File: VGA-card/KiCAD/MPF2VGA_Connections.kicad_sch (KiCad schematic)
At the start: 7 parts, among them J1 AppleIIBus, J2 VGA, J3 VGA, SW1 SW_Push

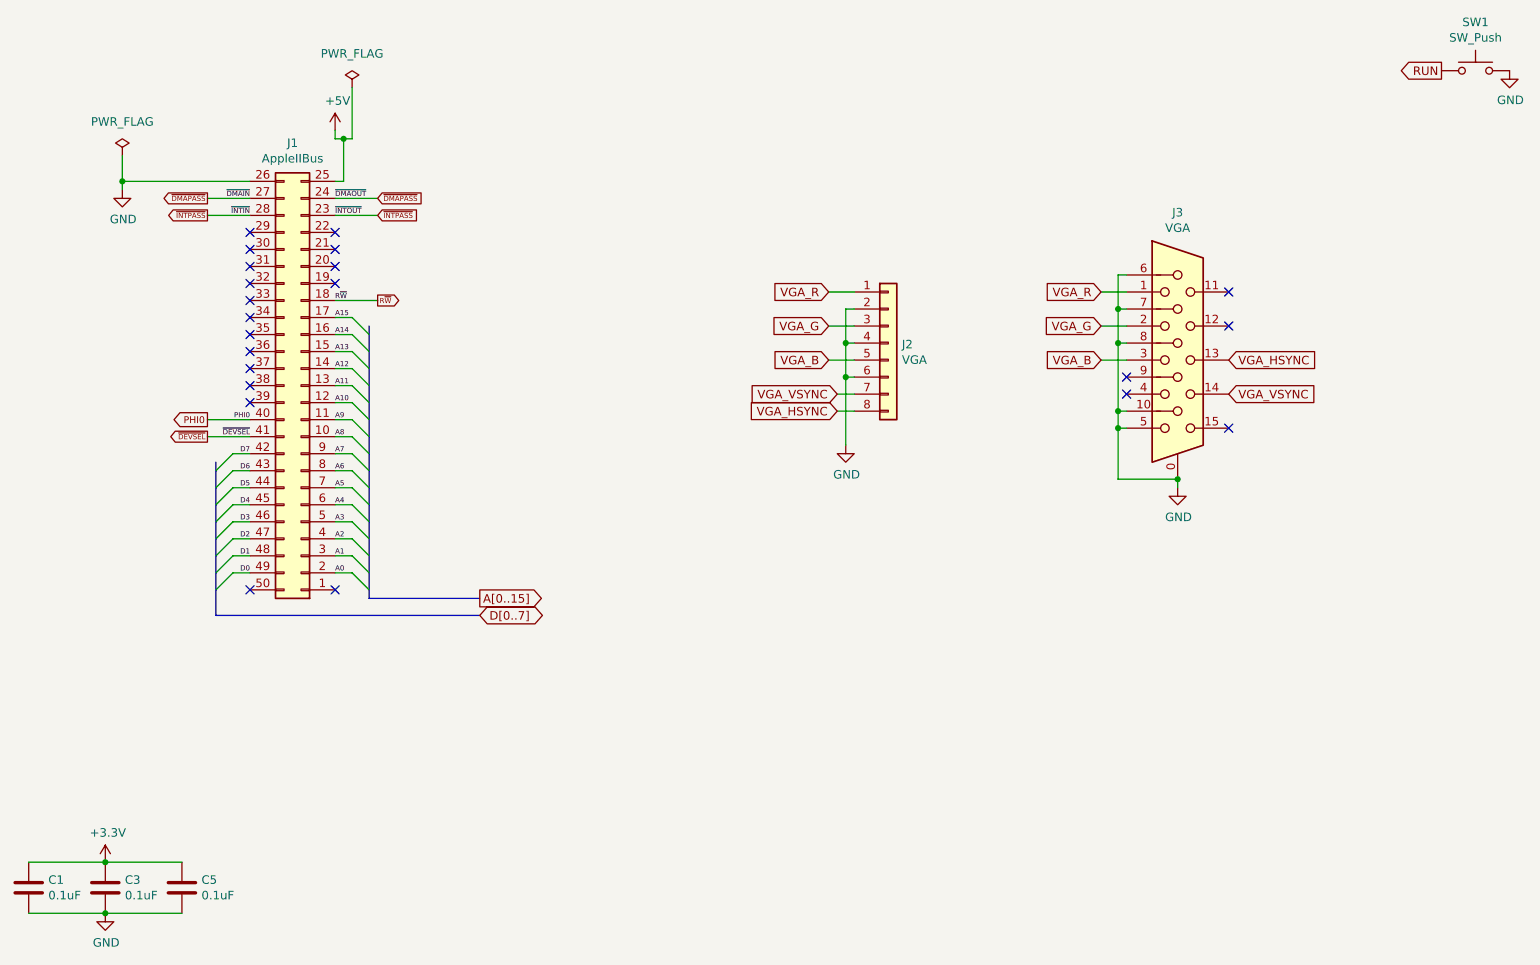
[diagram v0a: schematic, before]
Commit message: KiCAD connections sheet renamed
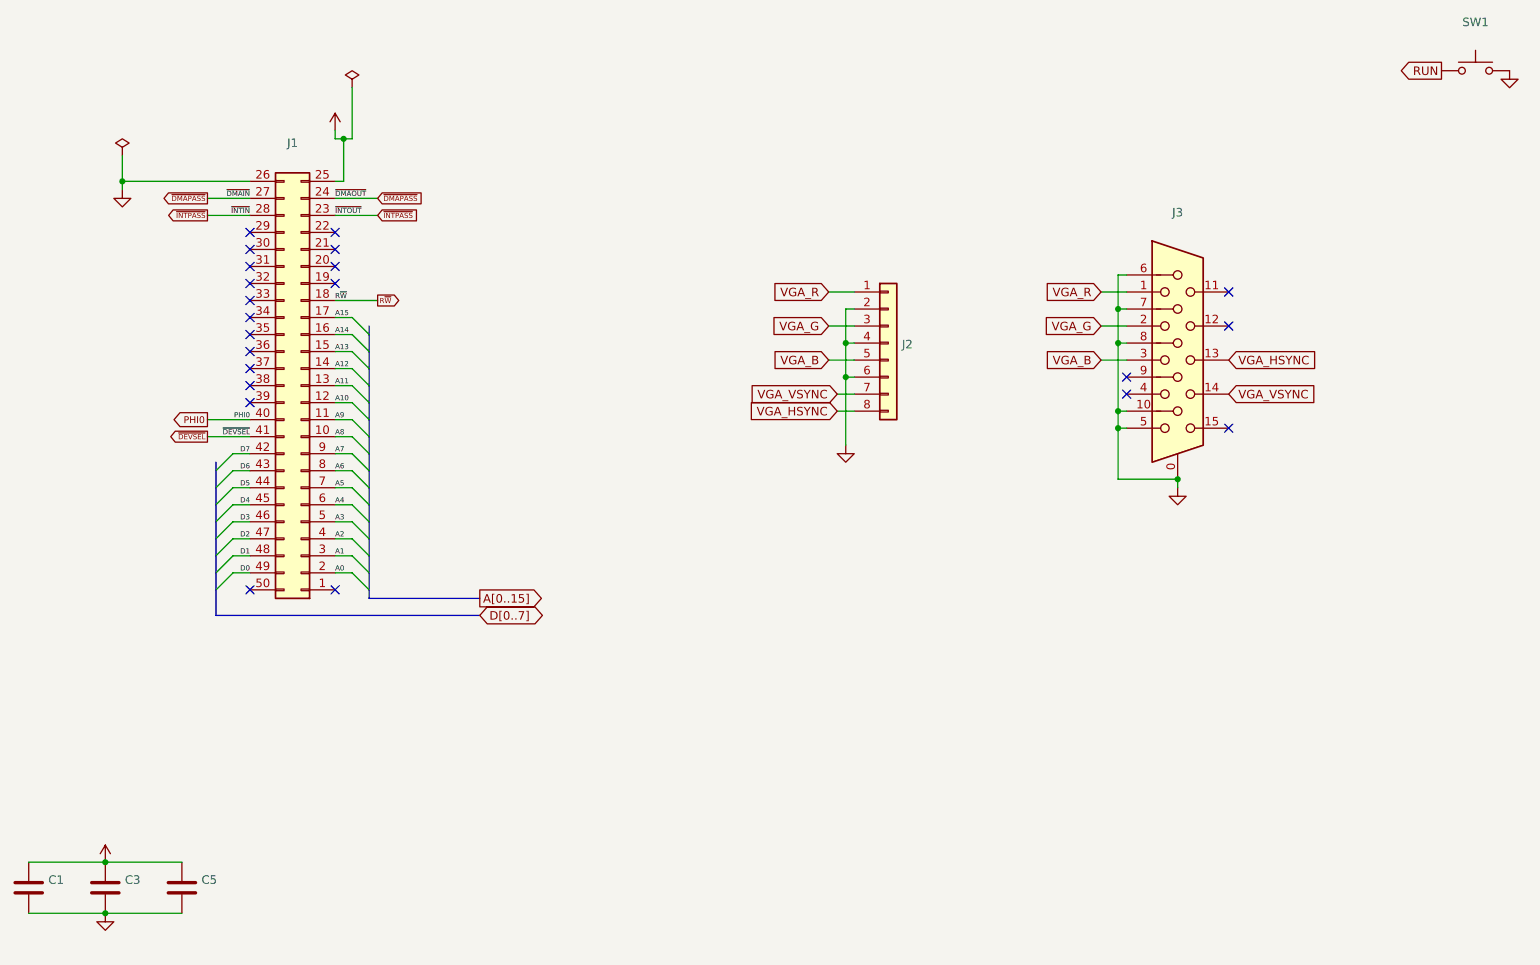
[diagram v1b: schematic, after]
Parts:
- C1, C3, C5: value 0.1uF -> (none); footprint Capacitor_THT:C_Disc_D4.3mm_W1.9mm_P5.00mm -> (none)
- J1: value AppleIIBus -> (none); footprint AppleVGA:AppleIIBus_Edge -> (none)
- J2: value VGA -> (none); footprint Connector_PinHeader_2.54mm:PinHeader_1x08_P2.54mm_Vertical -> (none)
- J3: value VGA -> (none); footprint Connector_Dsub:DSUB-15-HD_Female_Horizontal_P2.29x1.98mm_EdgePinOffset3.03mm_Housed_MountingHolesOffset4.94mm -> (none)
- SW1: value SW_Push -> (none); footprint Button_Switch_THT:SW_PUSH_6mm_H5mm -> (none)
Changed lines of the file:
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@@
       (effects (font (size 1.27 1.27)) (justify left))
     )
-    (property "Value" "0.1uF" (id 1) (at 30.861 171.323 0)
-      (effects (font (size 1.27 1.27)) (justify left))
-    )
-    (property "Footprint" "Capacitor_THT:C_Disc_D4.3mm_W1.9mm_P5.00mm" (id 2) (at 28.9052 173.99 0)
+    (property "Value" "" (id 1) (at 30.861 171.323 0)
+      (effects (font (size 1.27 1.27)) (justify left))
+    )
+    (property "Footprint" "" (id 2) (at 28.9052 173.99 0)
       (effects (font (size 1.27 1.27)) hide)
     )
@@
       (effects (font (size 1.27 1.27)) (justify left))
     )
-    (property "Value" "0.1uF" (id 1) (at 42.291 171.323 0)
-      (effects (font (size 1.27 1.27)) (justify left))
-    )
-    (property "Footprint" "Capacitor_THT:C_Disc_D4.3mm_W1.9mm_P5.00mm" (id 2) (at 40.3352 173.99 0)
+    (property "Value" "" (id 1) (at 42.291 171.323 0)
+      (effects (font (size 1.27 1.27)) (justify left))
+    )
+    (property "Footprint" "" (id 2) (at 40.3352 173.99 0)
       (effects (font (size 1.27 1.27)) hide)
     )
@@
       (effects (font (size 1.27 1.27)) (justify left))
     )
-    (property "Value" "0.1uF" (id 1) (at 53.721 171.323 0)
-      (effects (font (size 1.27 1.27)) (justify left))
-    )
-    (property "Footprint" "Capacitor_THT:C_Disc_D4.3mm_W1.9mm_P5.00mm" (id 2) (at 51.7652 173.99 0)
+    (property "Value" "" (id 1) (at 53.721 171.323 0)
+      (effects (font (size 1.27 1.27)) (justify left))
+    )
+    (property "Footprint" "" (id 2) (at 51.7652 173.99 0)
       (effects (font (size 1.27 1.27)) hide)
     )
@@
   (symbol (lib_id "power:+3.3V") (at 39.37 166.37 0) (unit 1)
     (in_bom yes) (on_board yes)
-    (property "Reference" "#PWR0115" (id 0) (at 39.37 170.18 0)
-      (effects (font (size 1.27 1.27)) hide)
-    )
-    (property "Value" "+3.3V" (id 1) (at 39.751 161.9758 0))
+    (property "Reference" "#PWR?" (id 0) (at 39.37 170.18 0)
+      (effects (font (size 1.27 1.27)) hide)
+    )
+    (property "Value" "" (id 1) (at 39.751 161.9758 0))
     (property "Footprint" "" (id 2) (at 39.37 166.37 0)
       (effects (font (size 1.27 1.27)) hide)
@@
   (symbol (lib_id "power:GND") (at 39.37 173.99 0) (unit 1)
     (in_bom yes) (on_board yes)
-    (property "Reference" "#PWR0116" (id 0) (at 39.37 180.34 0)
-      (effects (font (size 1.27 1.27)) hide)
-    )
-    (property "Value" "GND" (id 1) (at 39.497 178.3842 0))
+    (property "Reference" "#PWR?" (id 0) (at 39.37 180.34 0)
+      (effects (font (size 1.27 1.27)) hide)
+    )
+    (property "Value" "" (id 1) (at 39.497 178.3842 0))
     (property "Footprint" "" (id 2) (at 39.37 173.99 0)
       (effects (font (size 1.27 1.27)) hide)
@@
     (in_bom yes) (on_board yes)
     (property "Reference" "SW1" (id 0) (at 243.84 41.021 0))
-    (property "Value" "SW_Push" (id 1) (at 243.84 43.3324 0))
-    (property "Footprint" "Button_Switch_THT:SW_PUSH_6mm_H5mm" (id 2) (at 243.84 43.18 0)
+    (property "Value" "" (id 1) (at 243.84 43.3324 0))
+    (property "Footprint" "" (id 2) (at 243.84 43.18 0)
       (effects (font (size 1.27 1.27)) hide)
     )
@@
   (symbol (lib_id "power:GND") (at 248.92 48.26 0) (unit 1)
     (in_bom yes) (on_board yes)
-    (property "Reference" "#PWR0118" (id 0) (at 248.92 54.61 0)
-      (effects (font (size 1.27 1.27)) hide)
-    )
-    (property "Value" "GND" (id 1) (at 249.047 52.6542 0))
+    (property "Reference" "#PWR?" (id 0) (at 248.92 54.61 0)
+      (effects (font (size 1.27 1.27)) hide)
+    )
+    (property "Value" "" (id 1) (at 249.047 52.6542 0))
     (property "Footprint" "" (id 2) (at 248.92 48.26 0)
       (effects (font (size 1.27 1.27)) hide)
@@
       (effects (font (size 1.27 1.27)) (justify left))
     )
-    (property "Value" "VGA" (id 1) (at 158.242 91.4146 0)
-      (effects (font (size 1.27 1.27)) (justify left))
-    )
-    (property "Footprint" "Connector_PinHeader_2.54mm:PinHeader_1x08_P2.54mm_Vertical" (id 2) (at 156.21 88.9 0)
+    (property "Value" "" (id 1) (at 158.242 91.4146 0)
+      (effects (font (size 1.27 1.27)) (justify left))
+    )
+    (property "Footprint" "" (id 2) (at 156.21 88.9 0)
       (effects (font (size 1.27 1.27)) hide)
     )
@@
   (symbol (lib_id "power:GND") (at 149.86 104.14 0) (unit 1)
     (in_bom yes) (on_board yes)
-    (property "Reference" "#PWR0113" (id 0) (at 149.86 110.49 0)
-      (effects (font (size 1.27 1.27)) hide)
-    )
-    (property "Value" "GND" (id 1) (at 149.987 108.5342 0))
+    (property "Reference" "#PWR?" (id 0) (at 149.86 110.49 0)
+      (effects (font (size 1.27 1.27)) hide)
+    )
+    (property "Value" "" (id 1) (at 149.987 108.5342 0))
     (property "Footprint" "" (id 2) (at 149.86 104.14 0)
       (effects (font (size 1.27 1.27)) hide)
@@
   (symbol (lib_id "power:GND") (at 199.39 110.49 0) (unit 1)
     (in_bom yes) (on_board yes)
-    (property "Reference" "#PWR0114" (id 0) (at 199.39 116.84 0)
-      (effects (font (size 1.27 1.27)) hide)
-    )
-    (property "Value" "GND" (id 1) (at 199.517 114.8842 0))
+    (property "Reference" "#PWR?" (id 0) (at 199.39 116.84 0)
+      (effects (font (size 1.27 1.27)) hide)
+    )
+    (property "Value" "" (id 1) (at 199.517 114.8842 0))
     (property "Footprint" "" (id 2) (at 199.39 110.49 0)
       (effects (font (size 1.27 1.27)) hide)
@@
     (in_bom yes) (on_board yes)
     (property "Reference" "J3" (id 0) (at 199.39 69.4182 0))
-    (property "Value" "VGA" (id 1) (at 199.39 71.7296 0))
-    (property "Footprint" "Connector_Dsub:DSUB-15-HD_Female_Horizontal_P2.29x1.98mm_EdgePinOffset3.03mm_Housed_MountingHolesOffset4.94mm" (id 2) (at 175.26 81.28 0)
+    (property "Value" "" (id 1) (at 199.39 71.7296 0))
+    (property "Footprint" "" (id 2) (at 175.26 81.28 0)
       (effects (font (size 1.27 1.27)) hide)
     )
@@
     (in_bom yes) (on_board yes)
     (property "Reference" "J1" (id 0) (at 67.31 59.055 0))
-    (property "Value" "AppleIIBus" (id 1) (at 67.31 61.3664 0))
-    (property "Footprint" "AppleVGA:AppleIIBus_Edge" (id 2) (at 68.58 95.25 0)
+    (property "Value" "" (id 1) (at 67.31 61.3664 0))
+    (property "Footprint" "" (id 2) (at 68.58 95.25 0)
       (effects (font (size 1.27 1.27)) hide)
     )
@@
   (symbol (lib_id "power:GND") (at 41.91 66.04 0) (unit 1)
     (in_bom yes) (on_board yes)
-    (property "Reference" "#PWR0120" (id 0) (at 41.91 72.39 0)
-      (effects (font (size 1.27 1.27)) hide)
-    )
-    (property "Value" "GND" (id 1) (at 42.037 70.4342 0))
+    (property "Reference" "#PWR?" (id 0) (at 41.91 72.39 0)
+      (effects (font (size 1.27 1.27)) hide)
+    )
+    (property "Value" "" (id 1) (at 42.037 70.4342 0))
     (property "Footprint" "" (id 2) (at 41.91 66.04 0)
       (effects (font (size 1.27 1.27)) hide)
@@
   (symbol (lib_id "power:+5V") (at 73.66 57.15 0) (unit 1)
     (in_bom yes) (on_board yes)
-    (property "Reference" "#PWR0121" (id 0) (at 73.66 60.96 0)
-      (effects (font (size 1.27 1.27)) hide)
-    )
-    (property "Value" "+5V" (id 1) (at 74.041 52.7558 0))
+    (property "Reference" "#PWR?" (id 0) (at 73.66 60.96 0)
+      (effects (font (size 1.27 1.27)) hide)
+    )
+    (property "Value" "" (id 1) (at 74.041 52.7558 0))
     (property "Footprint" "" (id 2) (at 73.66 57.15 0)
       (effects (font (size 1.27 1.27)) hide)
@@
       (effects (font (size 1.27 1.27)) hide)
     )
-    (property "Value" "PWR_FLAG" (id 1) (at 76.2 45.72 0))
+    (property "Value" "" (id 1) (at 76.2 45.72 0))
     (property "Footprint" "" (id 2) (at 76.2 50.8 0)
       (effects (font (size 1.27 1.27)) hide)
@@
       (effects (font (size 1.27 1.27)) hide)
     )
-    (property "Value" "PWR_FLAG" (id 1) (at 41.91 55.88 0))
+    (property "Value" "" (id 1) (at 41.91 55.88 0))
     (property "Footprint" "" (id 2) (at 41.91 60.96 0)
       (effects (font (size 1.27 1.27)) hide)

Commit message: Schematics files updated
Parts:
- C1, C3, C5: value (none) -> 0.1uF; footprint (none) -> Capacitor_THT:C_Disc_D4.3mm_W1.9mm_P5.00mm
- J1: value (none) -> AppleIIBus; footprint (none) -> AppleVGA:AppleIIBus_Edge
- J2: value (none) -> VGA; footprint (none) -> Connector_PinHeader_2.54mm:PinHeader_1x08_P2.54mm_Vertical
- J3: value (none) -> VGA; footprint (none) -> Connector_Dsub:DSUB-15-HD_Female_Horizontal_P2.29x1.98mm_EdgePinOffset3.03mm_Housed_MountingHolesOffset4.94mm
- SW1: value (none) -> SW_Push; footprint (none) -> Button_Switch_THT:SW_PUSH_6mm_H5mm
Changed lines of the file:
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@@
       (effects (font (size 1.27 1.27)) (justify left))
     )
-    (property "Value" "" (id 1) (at 30.861 171.323 0)
-      (effects (font (size 1.27 1.27)) (justify left))
-    )
-    (property "Footprint" "" (id 2) (at 28.9052 173.99 0)
+    (property "Value" "0.1uF" (id 1) (at 30.861 171.323 0)
+      (effects (font (size 1.27 1.27)) (justify left))
+    )
+    (property "Footprint" "Capacitor_THT:C_Disc_D4.3mm_W1.9mm_P5.00mm" (id 2) (at 28.9052 173.99 0)
       (effects (font (size 1.27 1.27)) hide)
     )
@@
       (effects (font (size 1.27 1.27)) (justify left))
     )
-    (property "Value" "" (id 1) (at 42.291 171.323 0)
-      (effects (font (size 1.27 1.27)) (justify left))
-    )
-    (property "Footprint" "" (id 2) (at 40.3352 173.99 0)
+    (property "Value" "0.1uF" (id 1) (at 42.291 171.323 0)
+      (effects (font (size 1.27 1.27)) (justify left))
+    )
+    (property "Footprint" "Capacitor_THT:C_Disc_D4.3mm_W1.9mm_P5.00mm" (id 2) (at 40.3352 173.99 0)
       (effects (font (size 1.27 1.27)) hide)
     )
@@
       (effects (font (size 1.27 1.27)) (justify left))
     )
-    (property "Value" "" (id 1) (at 53.721 171.323 0)
-      (effects (font (size 1.27 1.27)) (justify left))
-    )
-    (property "Footprint" "" (id 2) (at 51.7652 173.99 0)
+    (property "Value" "0.1uF" (id 1) (at 53.721 171.323 0)
+      (effects (font (size 1.27 1.27)) (justify left))
+    )
+    (property "Footprint" "Capacitor_THT:C_Disc_D4.3mm_W1.9mm_P5.00mm" (id 2) (at 51.7652 173.99 0)
       (effects (font (size 1.27 1.27)) hide)
     )
@@
   (symbol (lib_id "power:+3.3V") (at 39.37 166.37 0) (unit 1)
     (in_bom yes) (on_board yes)
-    (property "Reference" "#PWR?" (id 0) (at 39.37 170.18 0)
-      (effects (font (size 1.27 1.27)) hide)
-    )
-    (property "Value" "" (id 1) (at 39.751 161.9758 0))
+    (property "Reference" "#PWR0113" (id 0) (at 39.37 170.18 0)
+      (effects (font (size 1.27 1.27)) hide)
+    )
+    (property "Value" "+3.3V" (id 1) (at 39.751 161.9758 0))
     (property "Footprint" "" (id 2) (at 39.37 166.37 0)
       (effects (font (size 1.27 1.27)) hide)
@@
   (symbol (lib_id "power:GND") (at 39.37 173.99 0) (unit 1)
     (in_bom yes) (on_board yes)
-    (property "Reference" "#PWR?" (id 0) (at 39.37 180.34 0)
-      (effects (font (size 1.27 1.27)) hide)
-    )
-    (property "Value" "" (id 1) (at 39.497 178.3842 0))
+    (property "Reference" "#PWR0114" (id 0) (at 39.37 180.34 0)
+      (effects (font (size 1.27 1.27)) hide)
+    )
+    (property "Value" "GND" (id 1) (at 39.497 178.3842 0))
     (property "Footprint" "" (id 2) (at 39.37 173.99 0)
       (effects (font (size 1.27 1.27)) hide)
@@
     (in_bom yes) (on_board yes)
     (property "Reference" "SW1" (id 0) (at 243.84 41.021 0))
-    (property "Value" "" (id 1) (at 243.84 43.3324 0))
-    (property "Footprint" "" (id 2) (at 243.84 43.18 0)
+    (property "Value" "SW_Push" (id 1) (at 243.84 43.3324 0))
+    (property "Footprint" "Button_Switch_THT:SW_PUSH_6mm_H5mm" (id 2) (at 243.84 43.18 0)
       (effects (font (size 1.27 1.27)) hide)
     )
@@
   (symbol (lib_id "power:GND") (at 248.92 48.26 0) (unit 1)
     (in_bom yes) (on_board yes)
-    (property "Reference" "#PWR?" (id 0) (at 248.92 54.61 0)
-      (effects (font (size 1.27 1.27)) hide)
-    )
-    (property "Value" "" (id 1) (at 249.047 52.6542 0))
+    (property "Reference" "#PWR0120" (id 0) (at 248.92 54.61 0)
+      (effects (font (size 1.27 1.27)) hide)
+    )
+    (property "Value" "GND" (id 1) (at 249.047 52.6542 0))
     (property "Footprint" "" (id 2) (at 248.92 48.26 0)
       (effects (font (size 1.27 1.27)) hide)
@@
       (effects (font (size 1.27 1.27)) (justify left))
     )
-    (property "Value" "" (id 1) (at 158.242 91.4146 0)
-      (effects (font (size 1.27 1.27)) (justify left))
-    )
-    (property "Footprint" "" (id 2) (at 156.21 88.9 0)
+    (property "Value" "VGA" (id 1) (at 158.242 91.4146 0)
+      (effects (font (size 1.27 1.27)) (justify left))
+    )
+    (property "Footprint" "Connector_PinHeader_2.54mm:PinHeader_1x08_P2.54mm_Vertical" (id 2) (at 156.21 88.9 0)
       (effects (font (size 1.27 1.27)) hide)
     )
@@
   (symbol (lib_id "power:GND") (at 149.86 104.14 0) (unit 1)
     (in_bom yes) (on_board yes)
-    (property "Reference" "#PWR?" (id 0) (at 149.86 110.49 0)
-      (effects (font (size 1.27 1.27)) hide)
-    )
-    (property "Value" "" (id 1) (at 149.987 108.5342 0))
+    (property "Reference" "#PWR0115" (id 0) (at 149.86 110.49 0)
+      (effects (font (size 1.27 1.27)) hide)
+    )
+    (property "Value" "GND" (id 1) (at 149.987 108.5342 0))
     (property "Footprint" "" (id 2) (at 149.86 104.14 0)
       (effects (font (size 1.27 1.27)) hide)
@@
   (symbol (lib_id "power:GND") (at 199.39 110.49 0) (unit 1)
     (in_bom yes) (on_board yes)
-    (property "Reference" "#PWR?" (id 0) (at 199.39 116.84 0)
-      (effects (font (size 1.27 1.27)) hide)
-    )
-    (property "Value" "" (id 1) (at 199.517 114.8842 0))
+    (property "Reference" "#PWR0121" (id 0) (at 199.39 116.84 0)
+      (effects (font (size 1.27 1.27)) hide)
+    )
+    (property "Value" "GND" (id 1) (at 199.517 114.8842 0))
     (property "Footprint" "" (id 2) (at 199.39 110.49 0)
       (effects (font (size 1.27 1.27)) hide)
@@
     (in_bom yes) (on_board yes)
     (property "Reference" "J3" (id 0) (at 199.39 69.4182 0))
-    (property "Value" "" (id 1) (at 199.39 71.7296 0))
-    (property "Footprint" "" (id 2) (at 175.26 81.28 0)
+    (property "Value" "VGA" (id 1) (at 199.39 71.7296 0))
+    (property "Footprint" "Connector_Dsub:DSUB-15-HD_Female_Horizontal_P2.29x1.98mm_EdgePinOffset3.03mm_Housed_MountingHolesOffset4.94mm" (id 2) (at 175.26 81.28 0)
       (effects (font (size 1.27 1.27)) hide)
     )
@@
     (in_bom yes) (on_board yes)
     (property "Reference" "J1" (id 0) (at 67.31 59.055 0))
-    (property "Value" "" (id 1) (at 67.31 61.3664 0))
-    (property "Footprint" "" (id 2) (at 68.58 95.25 0)
+    (property "Value" "AppleIIBus" (id 1) (at 67.31 61.3664 0))
+    (property "Footprint" "AppleVGA:AppleIIBus_Edge" (id 2) (at 68.58 95.25 0)
       (effects (font (size 1.27 1.27)) hide)
     )
@@
   (symbol (lib_id "power:GND") (at 41.91 66.04 0) (unit 1)
     (in_bom yes) (on_board yes)
-    (property "Reference" "#PWR?" (id 0) (at 41.91 72.39 0)
-      (effects (font (size 1.27 1.27)) hide)
-    )
-    (property "Value" "" (id 1) (at 42.037 70.4342 0))
+    (property "Reference" "#PWR0116" (id 0) (at 41.91 72.39 0)
+      (effects (font (size 1.27 1.27)) hide)
+    )
+    (property "Value" "GND" (id 1) (at 42.037 70.4342 0))
     (property "Footprint" "" (id 2) (at 41.91 66.04 0)
       (effects (font (size 1.27 1.27)) hide)
@@
   (symbol (lib_id "power:+5V") (at 73.66 57.15 0) (unit 1)
     (in_bom yes) (on_board yes)
-    (property "Reference" "#PWR?" (id 0) (at 73.66 60.96 0)
-      (effects (font (size 1.27 1.27)) hide)
-    )
-    (property "Value" "" (id 1) (at 74.041 52.7558 0))
+    (property "Reference" "#PWR0118" (id 0) (at 73.66 60.96 0)
+      (effects (font (size 1.27 1.27)) hide)
+    )
+    (property "Value" "+5V" (id 1) (at 74.041 52.7558 0))
     (property "Footprint" "" (id 2) (at 73.66 57.15 0)
       (effects (font (size 1.27 1.27)) hide)
@@
       (effects (font (size 1.27 1.27)) hide)
     )
-    (property "Value" "" (id 1) (at 76.2 45.72 0))
+    (property "Value" "PWR_FLAG" (id 1) (at 76.2 45.72 0))
     (property "Footprint" "" (id 2) (at 76.2 50.8 0)
       (effects (font (size 1.27 1.27)) hide)
@@
       (effects (font (size 1.27 1.27)) hide)
     )
-    (property "Value" "" (id 1) (at 41.91 55.88 0))
+    (property "Value" "PWR_FLAG" (id 1) (at 41.91 55.88 0))
     (property "Footprint" "" (id 2) (at 41.91 60.96 0)
       (effects (font (size 1.27 1.27)) hide)
